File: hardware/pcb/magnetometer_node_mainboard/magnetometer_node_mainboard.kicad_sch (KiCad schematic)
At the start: 0 parts

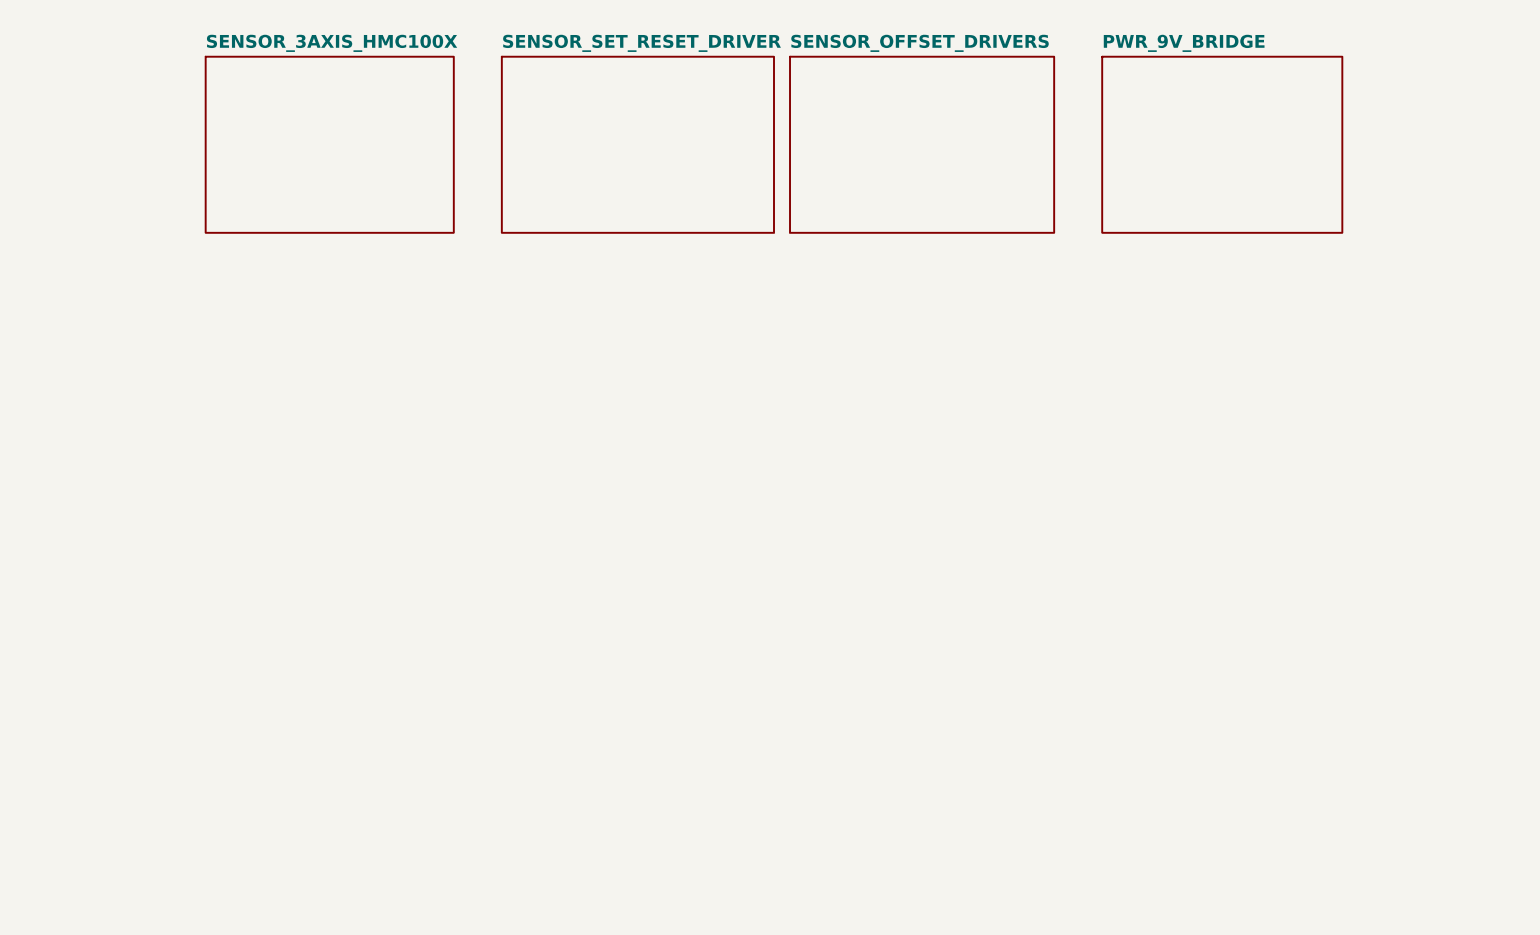
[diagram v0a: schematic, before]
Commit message: Schematic sensor stage done
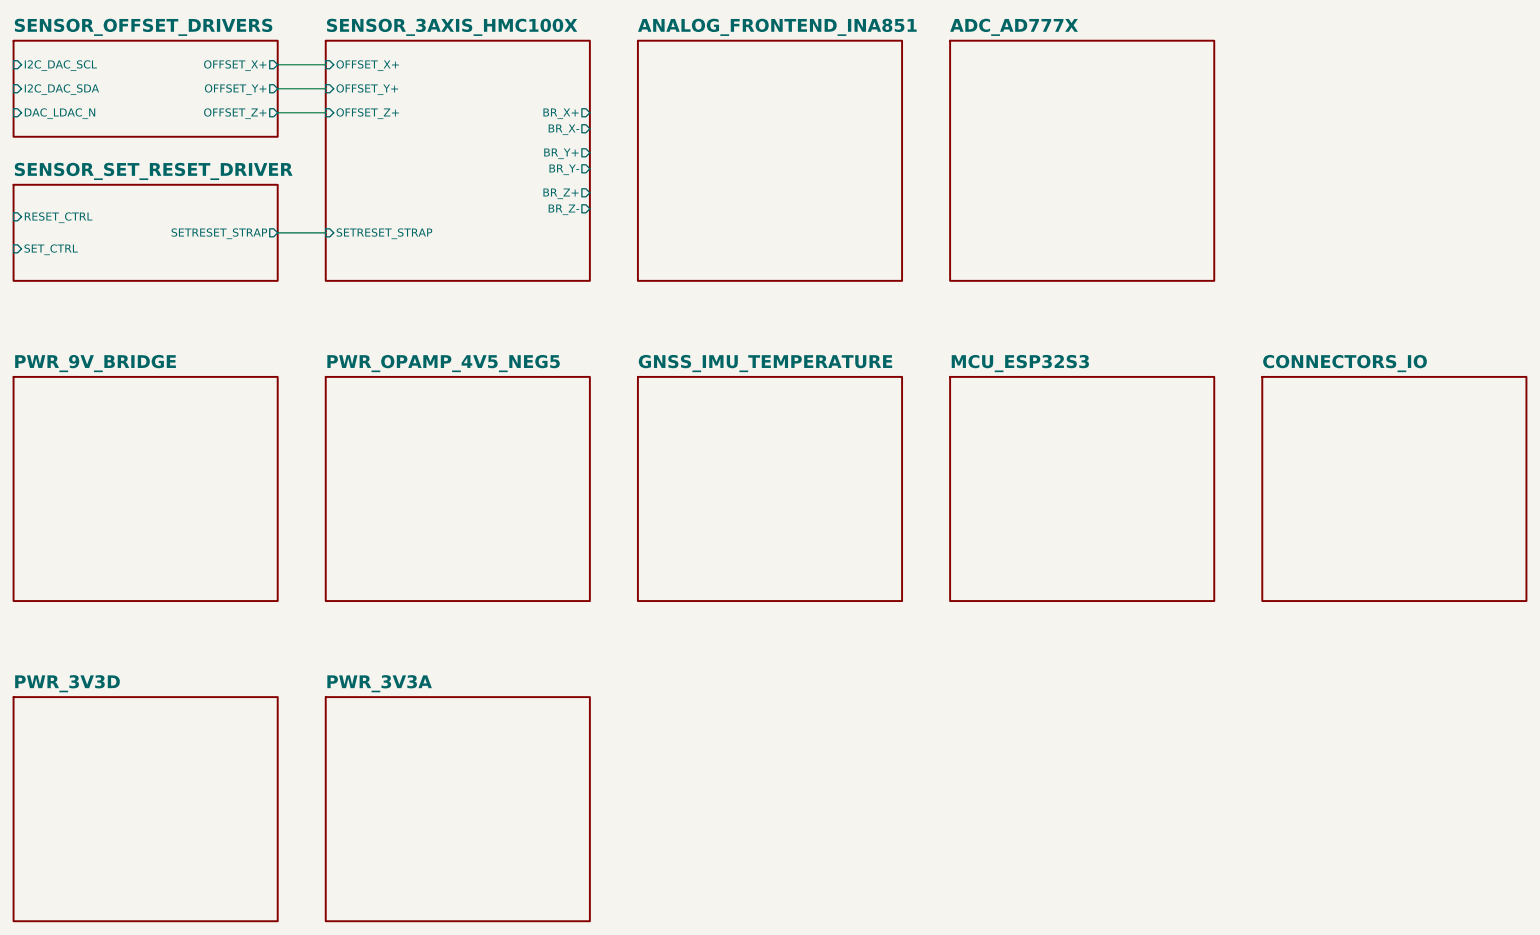
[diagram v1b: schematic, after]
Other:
- added sheet ADC_AD777X (schematics/adc_ad777x.kicad_sch)
- added sheet ANALOG_FRONTEND_INA851 (schematics/analog_frontend_ina851.kicad_sch)
- added sheet CONNECTORS_IO (schematics/connectors_io.kicad_sch)
- added sheet GNSS_IMU_TEMPERATURE (schematics/gnss_imu.kicad_sch)
- added sheet MCU_ESP32S3 (schematics/mcu_esp32s3.kicad_sch)
- added sheet PWR_3V3A (schematics/pwr_3v3a.kicad_sch)
- added sheet PWR_3V3D (schematics/pwr_3v3d.kicad_sch)
- added sheet PWR_OPAMP_4V5_NEG5 (schematics/pwr_opamp_4v5_neg5.kicad_sch)
- sheet SENSOR_3AXIS_HMC100X ports: added BR_X+, BR_X-, BR_Y+, BR_Y-, BR_Z+, BR_Z-, OFFSET_X+, OFFSET_Y+, OFFSET_Z+, SETRESET_STRAP; removed none
- sheet SENSOR_OFFSET_DRIVERS ports: added DAC_LDAC_N, I2C_DAC_SCL, I2C_DAC_SDA, OFFSET_X+, OFFSET_Y+, OFFSET_Z+; removed none
- sheet SENSOR_SET_RESET_DRIVER ports: added RESET_CTRL, SETRESET_STRAP, SET_CTRL; removed none
